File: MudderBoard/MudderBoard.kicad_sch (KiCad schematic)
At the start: 0 parts

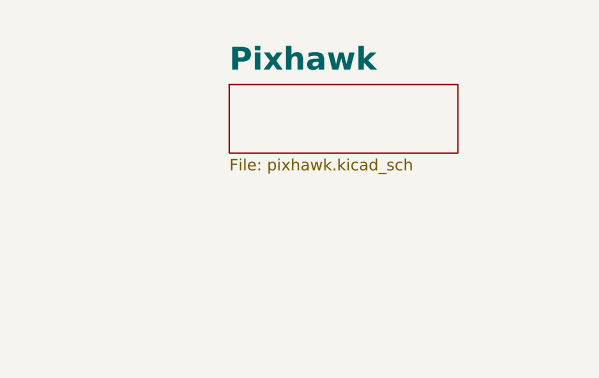
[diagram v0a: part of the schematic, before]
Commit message: ESC Boost Converter THT
Designing new THT boost converter.
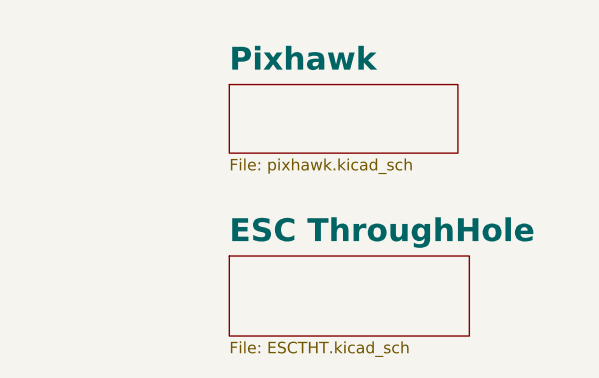
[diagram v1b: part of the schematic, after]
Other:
- added sheet ESC ThroughHole (ESCTHT.kicad_sch)
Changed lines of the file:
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@@
+	)
+	(sheet
+		(at 234.95 133.35)
+		(size 26.67 8.89)
+		(fields_autoplaced yes)
+		(stroke
+			(width 0.1524)
+			(type solid)
+		)
+		(fill
+			(color 0 0 0 0.0000)
+		)
+		(property "Sheetname" "ESC ThroughHole"
+			(at 234.95 132.0034 0)
+			(effects
+				(font
+					(size 2.54 2.54)
+					(bold yes)
+				)
+				(justify left bottom)
+			)
+		)
+		(property "Sheetfile" "ESCTHT.kicad_sch"
+			(at 234.95 142.8246 0)
+			(effects
+				(font
+					(size 1.27 1.27)
+				)
+				(justify left top)
+			)
+		)
+		(instances
+			(project "MudderBoard"
+				(path "/cdf98bf7-80ce-4b13-b655-e6c7c589c122"
+					(page "7")
+				)
+			)
+		)
 	)
 	(sheet

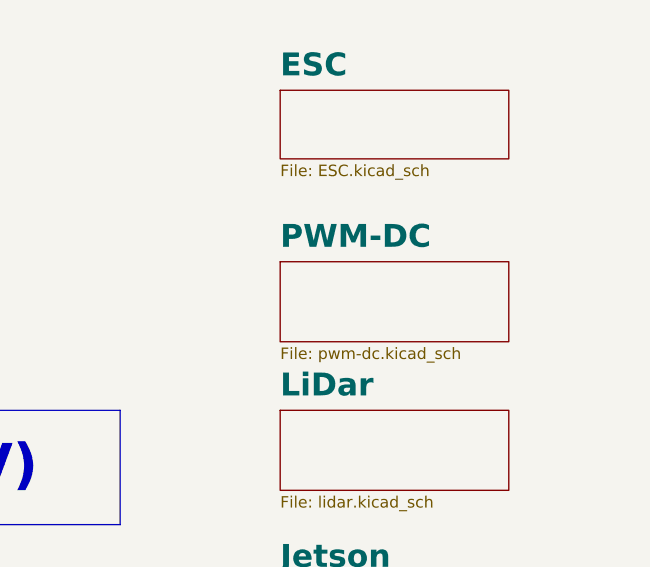
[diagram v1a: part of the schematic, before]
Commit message: Updated Lidar Circuit
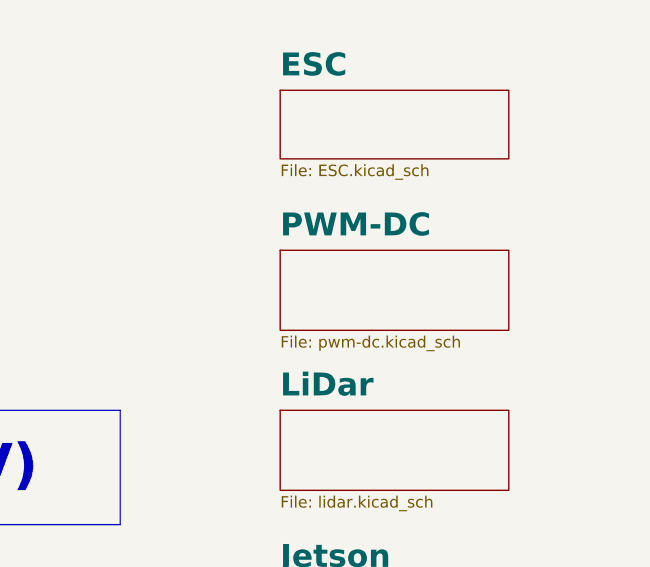
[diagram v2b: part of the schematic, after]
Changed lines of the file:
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@@
 	)
 	(sheet
-		(at 234.95 55.88)
+		(at 234.95 54.61)
 		(size 25.4 8.89)
 		(fields_autoplaced yes)
@@
 		)
 		(property "Sheetname" "PWM-DC"
-			(at 234.95 54.5334 0)
+			(at 234.95 53.2634 0)
 			(effects
 				(font
@@
 		)
 		(property "Sheetfile" "pwm-dc.kicad_sch"
-			(at 234.95 65.3546 0)
+			(at 234.95 64.0846 0)
 			(effects
 				(font

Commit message: added jetson circuit
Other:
- removed sheet ESC ThroughHole
- added sheet Legend (legend.kicad_sch)
- sheet ESC: file ESC.kicad_sch -> ESCTHT.kicad_sch
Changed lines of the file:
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@@
 	(polyline
 		(pts
-			(xy 93.98 74.93) (xy 109.22 74.93)
+			(xy 92.71 88.9) (xy 107.95 88.9)
 		)
 		(stroke
@@
 	(polyline
 		(pts
-			(xy 72.39 58.42) (xy 144.78 58.42)
+			(xy 71.12 72.39) (xy 143.51 72.39)
 		)
 		(stroke
@@
 	(polyline
 		(pts
-			(xy 167.64 49.53) (xy 167.64 55.88)
+			(xy 166.37 63.5) (xy 166.37 69.85)
 		)
 		(stroke
@@
 	(polyline
 		(pts
-			(xy 72.39 29.21) (xy 157.48 29.21)
+			(xy 71.12 43.18) (xy 156.21 43.18)
 		)
 		(stroke
@@
 	(polyline
 		(pts
-			(xy 101.6 69.85) (xy 101.6 43.18)
+			(xy 100.33 83.82) (xy 100.33 57.15)
 		)
 		(stroke
@@
 	(polyline
 		(pts
-			(xy 109.22 74.93) (xy 109.22 64.77)
+			(xy 107.95 88.9) (xy 107.95 78.74)
 		)
 		(stroke
@@
 	(polyline
 		(pts
-			(xy 109.22 64.77) (xy 144.78 64.77)
+			(xy 107.95 78.74) (xy 143.51 78.74)
 		)
 		(stroke
@@
 	(polyline
 		(pts
-			(xy 157.48 29.21) (xy 157.48 36.83)
+			(xy 156.21 43.18) (xy 156.21 50.8)
 		)
 		(stroke
@@
 	(polyline
 		(pts
-			(xy 144.78 57.15) (xy 144.78 58.42)
+			(xy 143.51 71.12) (xy 143.51 72.39)
 		)
 		(stroke
@@
 	(polyline
 		(pts
-			(xy 90.17 90.17) (xy 90.17 116.84)
+			(xy 88.9 104.14) (xy 88.9 130.81)
 		)
 		(stroke
@@
 	(polyline
 		(pts
-			(xy 93.98 78.74) (xy 144.78 78.74)
+			(xy 92.71 92.71) (xy 143.51 92.71)
 		)
 		(stroke
@@
 	(polyline
 		(pts
-			(xy 134.62 116.84) (xy 144.78 116.84)
+			(xy 133.35 130.81) (xy 143.51 130.81)
 		)
 		(stroke
@@
 	(polyline
 		(pts
-			(xy 90.17 116.84) (xy 134.62 116.84)
+			(xy 88.9 130.81) (xy 133.35 130.81)
 		)
 		(stroke
@@
 	(polyline
 		(pts
-			(xy 166.37 19.05) (xy 166.37 36.83)
+			(xy 165.1 33.02) (xy 165.1 50.8)
 		)
 		(stroke
@@
 	(polyline
 		(pts
-			(xy 72.39 19.05) (xy 166.37 19.05)
+			(xy 71.12 33.02) (xy 165.1 33.02)
 		)
 		(stroke
@@
 	(polyline
 		(pts
-			(xy 144.78 99.06) (xy 109.22 99.06)
+			(xy 143.51 113.03) (xy 107.95 113.03)
 		)
 		(stroke
@@
 	(polyline
 		(pts
-			(xy 109.22 99.06) (xy 109.22 83.82)
+			(xy 107.95 113.03) (xy 107.95 97.79)
 		)
 		(stroke
@@
 	(polyline
 		(pts
-			(xy 93.98 69.85) (xy 101.6 69.85)
+			(xy 92.71 83.82) (xy 100.33 83.82)
 		)
 		(stroke
@@
 	(polyline
 		(pts
-			(xy 101.6 43.18) (xy 144.78 43.18)
+			(xy 100.33 57.15) (xy 143.51 57.15)
 		)
 		(stroke
@@
 	(polyline
 		(pts
-			(xy 93.98 83.82) (xy 109.22 83.82)
+			(xy 92.71 97.79) (xy 107.95 97.79)
 		)
 		(stroke
@@
 	(text_box "PWM CH2"
 		(exclude_from_sim no)
-		(at 31.75 16.51 0)
+		(at 30.48 30.48 0)
 		(size 40.64 6.35)
 		(stroke
@@
 	(text_box "PWM CH5"
 		(exclude_from_sim no)
-		(at 31.75 54.61 0)
+		(at 30.48 68.58 0)
 		(size 40.64 6.35)
 		(stroke
@@
 	(text_box "Pixhawk (5V)"
 		(exclude_from_sim no)
-		(at 144.78 111.76 0)
+		(at 143.51 125.73 0)
 		(size 52.07 12.7)
 		(stroke
@@
 	(text_box "Jetson (12V)"
 		(exclude_from_sim no)
-		(at 144.78 91.44 0)
+		(at 143.51 105.41 0)
 		(size 50.8 12.7)
 		(stroke
@@
 	(text_box "LiDar + Wifi(24V)"
 		(exclude_from_sim no)
-		(at 144.78 72.39 0)
+		(at 143.51 86.36 0)
 		(size 72.39 12.7)
 		(stroke
@@
 	(text_box "PWM-DC"
 		(exclude_from_sim no)
-		(at 144.78 55.88 0)
+		(at 143.51 69.85 0)
 		(size 44.45 12.7)
 		(stroke
@@
 	(text_box "ESC (20V)"
 		(exclude_from_sim no)
-		(at 144.78 36.83 0)
+		(at 143.51 50.8 0)
 		(size 44.45 12.7)
 		(stroke
@@
 	(text_box "Battery Supply (14.8V Nominal)"
 		(exclude_from_sim no)
-		(at 22.86 67.31 0)
+		(at 21.59 81.28 0)
 		(size 71.12 22.86)
 		(stroke
@@
 	(text_box "PWM CH3"
 		(exclude_from_sim no)
-		(at 31.75 26.67 0)
+		(at 30.48 40.64 0)
 		(size 40.64 6.35)
 		(stroke
@@
 	(text "VCC"
 		(exclude_from_sim no)
-		(at 115.57 63.246 0)
+		(at 114.3 77.216 0)
 		(effects
 			(font
@@
 	(text "PWM_CH3"
 		(exclude_from_sim no)
-		(at 86.106 27.686 0)
+		(at 84.836 41.656 0)
 		(effects
 			(font
@@
 	(text "VCC"
 		(exclude_from_sim no)
-		(at 115.316 77.47 0)
+		(at 114.046 91.44 0)
 		(effects
 			(font
@@
 	(text "PWM_CH2"
 		(exclude_from_sim no)
-		(at 86.868 17.018 0)
+		(at 85.598 30.988 0)
 		(effects
 			(font
@@
 	(text "PWM_CH5"
 		(exclude_from_sim no)
-		(at 85.344 56.896 0)
+		(at 84.074 70.866 0)
 		(effects
 			(font
@@
 	(text "VCC"
 		(exclude_from_sim no)
-		(at 115.57 97.282 0)
+		(at 114.3 111.252 0)
 		(effects
 			(font
@@
 	(text "Schematic:"
 		(exclude_from_sim no)
-		(at 247.65 20.574 0)
+		(at 246.38 21.844 0)
 		(effects
 			(font
@@
 	(text "VCC"
 		(exclude_from_sim no)
-		(at 113.538 41.656 0)
+		(at 112.268 55.626 0)
 		(effects
 			(font
@@
 	(text "VCC"
 		(exclude_from_sim no)
-		(at 96.774 115.316 0)
+		(at 95.504 129.286 0)
 		(effects
 			(font
@@
 	)
 	(sheet
-		(at 234.95 114.3)
-		(size 25.4 7.62)
-		(fields_autoplaced yes)
+		(at 232.41 113.03)
+		(size 25.4 11.43)
 		(stroke
 			(width 0.1524)
@@
 		)
 		(property "Sheetname" "Pixhawk"
-			(at 234.95 112.9534 0)
+			(at 231.648 112.014 0)
 			(effects
 				(font
@@
 		)
 		(property "Sheetfile" "pixhawk.kicad_sch"
-			(at 234.95 122.5046 0)
+			(at 232.41 125.222 0)
 			(effects
 				(font
@@
 	)
 	(sheet
-		(at 234.95 133.35)
+		(at 232.41 135.89)
 		(size 26.67 8.89)
-		(fields_autoplaced yes)
 		(stroke
 			(width 0.1524)
@@
 			(color 0 0 0 0.0000)
 		)
-		(property "Sheetname" "ESC ThroughHole"
-			(at 234.95 132.0034 0)
+		(property "Sheetname" "ESC"
+			(at 231.648 134.62 0)
 			(effects
 				(font
@@
 		)
 		(property "Sheetfile" "ESCTHT.kicad_sch"
-			(at 234.95 142.8246 0)
+			(at 232.41 145.3646 0)
 			(effects
 				(font
@@
 	)
 	(sheet
-		(at 234.95 54.61)
+		(at 232.41 57.15)
 		(size 25.4 8.89)
 		(fields_autoplaced yes)
@@
 		)
 		(property "Sheetname" "PWM-DC"
-			(at 234.95 53.2634 0)
+			(at 232.41 55.8034 0)
 			(effects
 				(font
@@
 		)
 		(property "Sheetfile" "pwm-dc.kicad_sch"
-			(at 234.95 64.0846 0)
+			(at 232.41 66.6246 0)
 			(effects
 				(font
@@
 	)
 	(sheet
-		(at 234.95 36.83)
-		(size 25.4 7.62)
+		(at 232.41 93.98)
+		(size 25.4 8.89)
 		(fields_autoplaced yes)
 		(stroke
@@
 			(color 0 0 0 0.0000)
 		)
-		(property "Sheetname" "ESC"
-			(at 234.95 35.4834 0)
+		(property "Sheetname" "Jetson"
+			(at 232.41 92.6334 0)
 			(effects
 				(font
@@
 			)
 		)
-		(property "Sheetfile" "ESC.kicad_sch"
-			(at 234.95 45.0346 0)
+		(property "Sheetfile" "jetson.kicad_sch"
+			(at 232.41 103.4546 0)
 			(effects
 				(font
@@
 			(project "MudderBoard"
 				(path "/cdf98bf7-80ce-4b13-b655-e6c7c589c122"
-					(page "3")
+					(page "5")
 				)
 			)
@@
 	)
 	(sheet
-		(at 234.95 91.44)
-		(size 25.4 8.89)
+		(at 232.41 35.56)
+		(size 25.4 12.7)
 		(fields_autoplaced yes)
 		(stroke
@@
 			(color 0 0 0 0.0000)
 		)
-		(property "Sheetname" "Jetson"
-			(at 234.95 90.0934 0)
+		(property "Sheetname" "Legend"
+			(at 232.41 34.2134 0)
 			(effects
 				(font
@@
 			)
 		)
-		(property "Sheetfile" "jetson.kicad_sch"
-			(at 234.95 100.9146 0)
+		(property "Sheetfile" "legend.kicad_sch"
+			(at 232.41 48.8446 0)
 			(effects
 				(font
@@
 			(project "MudderBoard"
 				(path "/cdf98bf7-80ce-4b13-b655-e6c7c589c122"
-					(page "5")
+					(page "7")
 				)
 			)
@@
 	)
 	(sheet
-		(at 234.95 72.39)
+		(at 232.41 74.93)
 		(size 25.4 8.89)
 		(fields_autoplaced yes)
@@
 		)
 		(property "Sheetname" "LiDar"
-			(at 234.95 71.0434 0)
+			(at 232.41 73.5834 0)
 			(effects
 				(font
@@
 		)
 		(property "Sheetfile" "lidar.kicad_sch"
-			(at 234.95 81.8646 0)
+			(at 232.41 84.4046 0)
 			(effects
 				(font

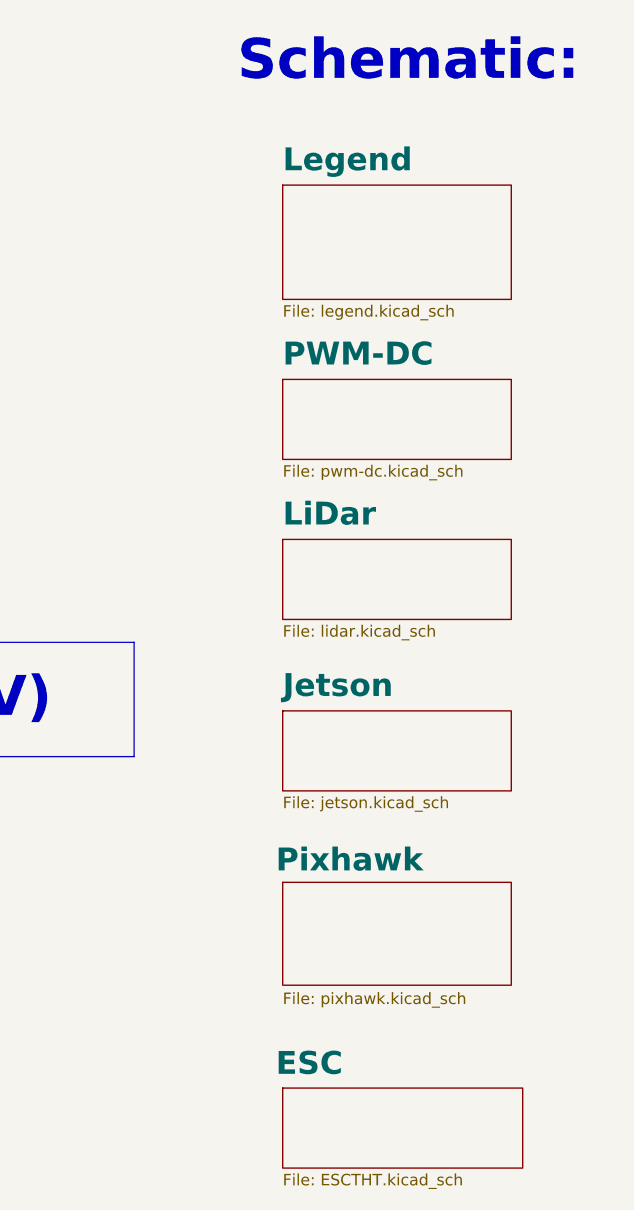
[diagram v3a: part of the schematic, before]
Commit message: AddedPWM-DC footprints
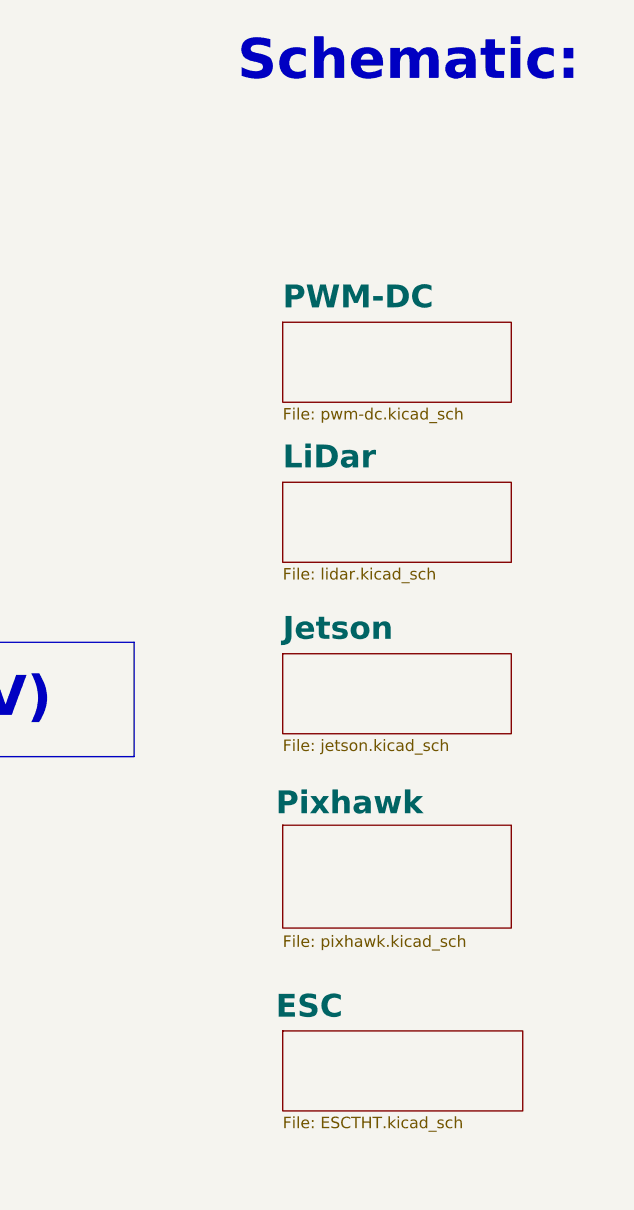
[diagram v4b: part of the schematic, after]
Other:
- removed sheet Legend
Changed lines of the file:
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@@
 	)
 	(sheet
-		(at 232.41 113.03)
+		(at 232.41 106.68)
 		(size 25.4 11.43)
 		(stroke
@@
 		)
 		(property "Sheetname" "Pixhawk"
-			(at 231.648 112.014 0)
+			(at 231.648 105.664 0)
 			(effects
 				(font
@@
 		)
 		(property "Sheetfile" "pixhawk.kicad_sch"
-			(at 232.41 125.222 0)
+			(at 232.41 118.872 0)
 			(effects
 				(font
@@
 	)
 	(sheet
-		(at 232.41 135.89)
+		(at 232.41 129.54)
 		(size 26.67 8.89)
 		(stroke
@@
 		)
 		(property "Sheetname" "ESC"
-			(at 231.648 134.62 0)
+			(at 231.648 128.27 0)
 			(effects
 				(font
@@
 		)
 		(property "Sheetfile" "ESCTHT.kicad_sch"
-			(at 232.41 145.3646 0)
+			(at 232.41 139.0146 0)
 			(effects
 				(font
@@
 	)
 	(sheet
-		(at 232.41 57.15)
+		(at 232.41 50.8)
 		(size 25.4 8.89)
 		(fields_autoplaced yes)
@@
 		)
 		(property "Sheetname" "PWM-DC"
-			(at 232.41 55.8034 0)
+			(at 232.41 49.4534 0)
 			(effects
 				(font
@@
 		)
 		(property "Sheetfile" "pwm-dc.kicad_sch"
-			(at 232.41 66.6246 0)
+			(at 232.41 60.2746 0)
 			(effects
 				(font
@@
 	)
 	(sheet
-		(at 232.41 93.98)
+		(at 232.41 87.63)
 		(size 25.4 8.89)
 		(fields_autoplaced yes)
@@
 		)
 		(property "Sheetname" "Jetson"
-			(at 232.41 92.6334 0)
+			(at 232.41 86.2834 0)
 			(effects
 				(font
@@
 		)
 		(property "Sheetfile" "jetson.kicad_sch"
-			(at 232.41 103.4546 0)
+			(at 232.41 97.1046 0)
 			(effects
 				(font
@@
 	)
 	(sheet
-		(at 232.41 35.56)
-		(size 25.4 12.7)
-		(fields_autoplaced yes)
-		(stroke
-			(width 0.1524)
-			(type solid)
-		)
-		(fill
-			(color 0 0 0 0.0000)
-		)
-		(property "Sheetname" "Legend"
-			(at 232.41 34.2134 0)
-			(effects
-				(font
-					(size 2.54 2.54)
-					(bold yes)
-				)
-				(justify left bottom)
-			)
-		)
-		(property "Sheetfile" "legend.kicad_sch"
-			(at 232.41 48.8446 0)
-			(effects
-				(font
-					(size 1.27 1.27)
-				)
-				(justify left top)
-			)
-		)
-		(instances
-			(project "MudderBoard"
-				(path "/cdf98bf7-80ce-4b13-b655-e6c7c589c122"
-					(page "7")
-				)
-			)
-		)
-	)
-	(sheet
-		(at 232.41 74.93)
+		(at 232.41 68.58)
 		(size 25.4 8.89)
 		(fields_autoplaced yes)
@@
 		)
 		(property "Sheetname" "LiDar"
-			(at 232.41 73.5834 0)
+			(at 232.41 67.2334 0)
 			(effects
 				(font
@@
 		)
 		(property "Sheetfile" "lidar.kicad_sch"
-			(at 232.41 84.4046 0)
+			(at 232.41 78.0546 0)
 			(effects
 				(font
